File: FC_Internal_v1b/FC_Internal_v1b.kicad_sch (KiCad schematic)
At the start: 97 parts, among them IC1 RP2040_QFN56, IC2 AZ1117CH-3.3TRG1, J1 Conn_ARM_JTAG_SWD_10, J10 BM04B-SRSS-TB(LF)(SN), J11 BM04B-SRSS-TB(LF)(SN), J12 BM04B-SRSS-TB(LF)(SN), J13 Breakout, J15 Battery, J15 Breakout, J16 Debug, J2 FC to EPS Connector, J3 Life Makes Lemonade, J4 104031-0811, J5 BM04B-SRSS-TB(LF)(SN), J6 Conn_Coaxial, J7 Breakout, J8 USB_B_Micro, J9 BM04B-SRSS-TB(LF)(SN), SW1 KMR2, SW2 KMR2, U10 AP3602AKTR-G1, U3 MAX706RESA, U4 RFM98PW, U5 RFM9xBreakout, U6 W25Q128JV, U7 LSM6DSOTR, U8 LSM303AGRTR, U9 MCP25625-E/ML, Y1 12MHZ, Y3 16MHZ 12 pf

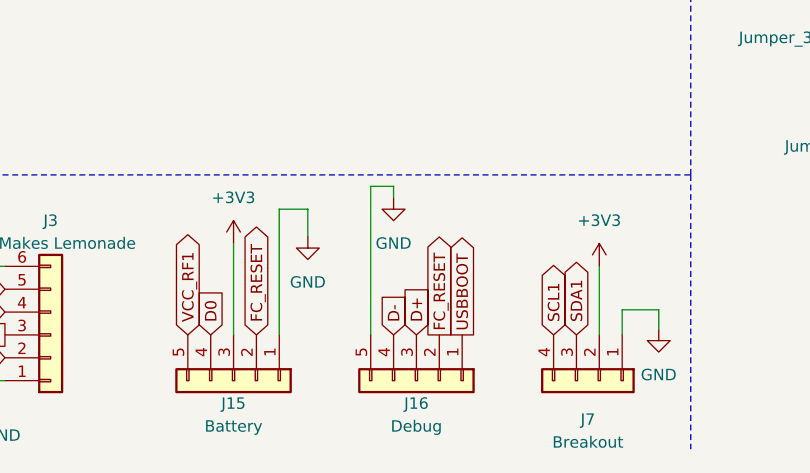
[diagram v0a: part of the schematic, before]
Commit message: Added 5pos Debug Connector to Layout
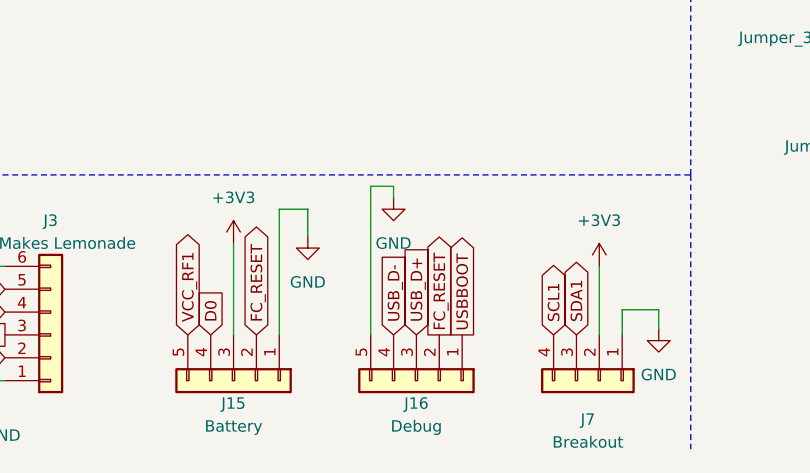
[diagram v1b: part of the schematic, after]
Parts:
- J7: footprint Connector_JST:JST_SH_SM04B-SRSS-TB_1x04-1MP_P1.00mm_Horizontal -> FC_DEV_BOARD:JST_BM04B-SRSS-TB(LF)(SN)
- J9: footprint FC_DEV_BOARD:JST_BM04B-SRSS-TB(LF)(SN) -> FC_DEV_BOARD:JST_BM04B-SRSS-TB(LF)(SN)
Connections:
- net D+: no longer J16.3 (Pin_3)
- net D-: no longer J16.4 (Pin_4)
- net USB_D+: now also J16.3 (Pin_3)
- net USB_D-: now also J16.4 (Pin_4)
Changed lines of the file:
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@@
 		)
 	)
-	(global_label "D-"
+	(global_label "USB_D-"
 		(shape input)
 		(at 156.21 271.78 90)
@@
 		)
 		(property "Intersheetrefs" "${INTERSHEET_REFS}"
-			(at 156.21 265.9524 90)
+			(at 156.21 261.1748 90)
 			(effects
 				(font
@@
 		)
 	)
-	(global_label "D+"
+	(global_label "USB_D+"
 		(shape input)
 		(at 158.75 271.78 90)
@@
 		)
 		(property "Intersheetrefs" "${INTERSHEET_REFS}"
-			(at 158.75 265.9524 90)
+			(at 158.75 261.1748 90)
 			(effects
 				(font
@@
 			)
 		)
-		(property "Footprint" "Connector_JST:JST_SH_SM04B-SRSS-TB_1x04-1MP_P1.00mm_Horizontal"
+		(property "Footprint" "FC_DEV_BOARD:JST_BM04B-SRSS-TB(LF)(SN)"
 			(at 179.07 276.86 0)
 			(effects
@@
 			)
 		)
-		(property "Footprint" "FC_DEV_BOARD:JST_BM04B-SRSS-TB(LF)(SN)"
+		(property "Footprint" "FC_DEV_BOARD:JST_BM04B-SRSS-TB(LF)(SN) "
 			(at 181.61 63.5 0)
 			(effects

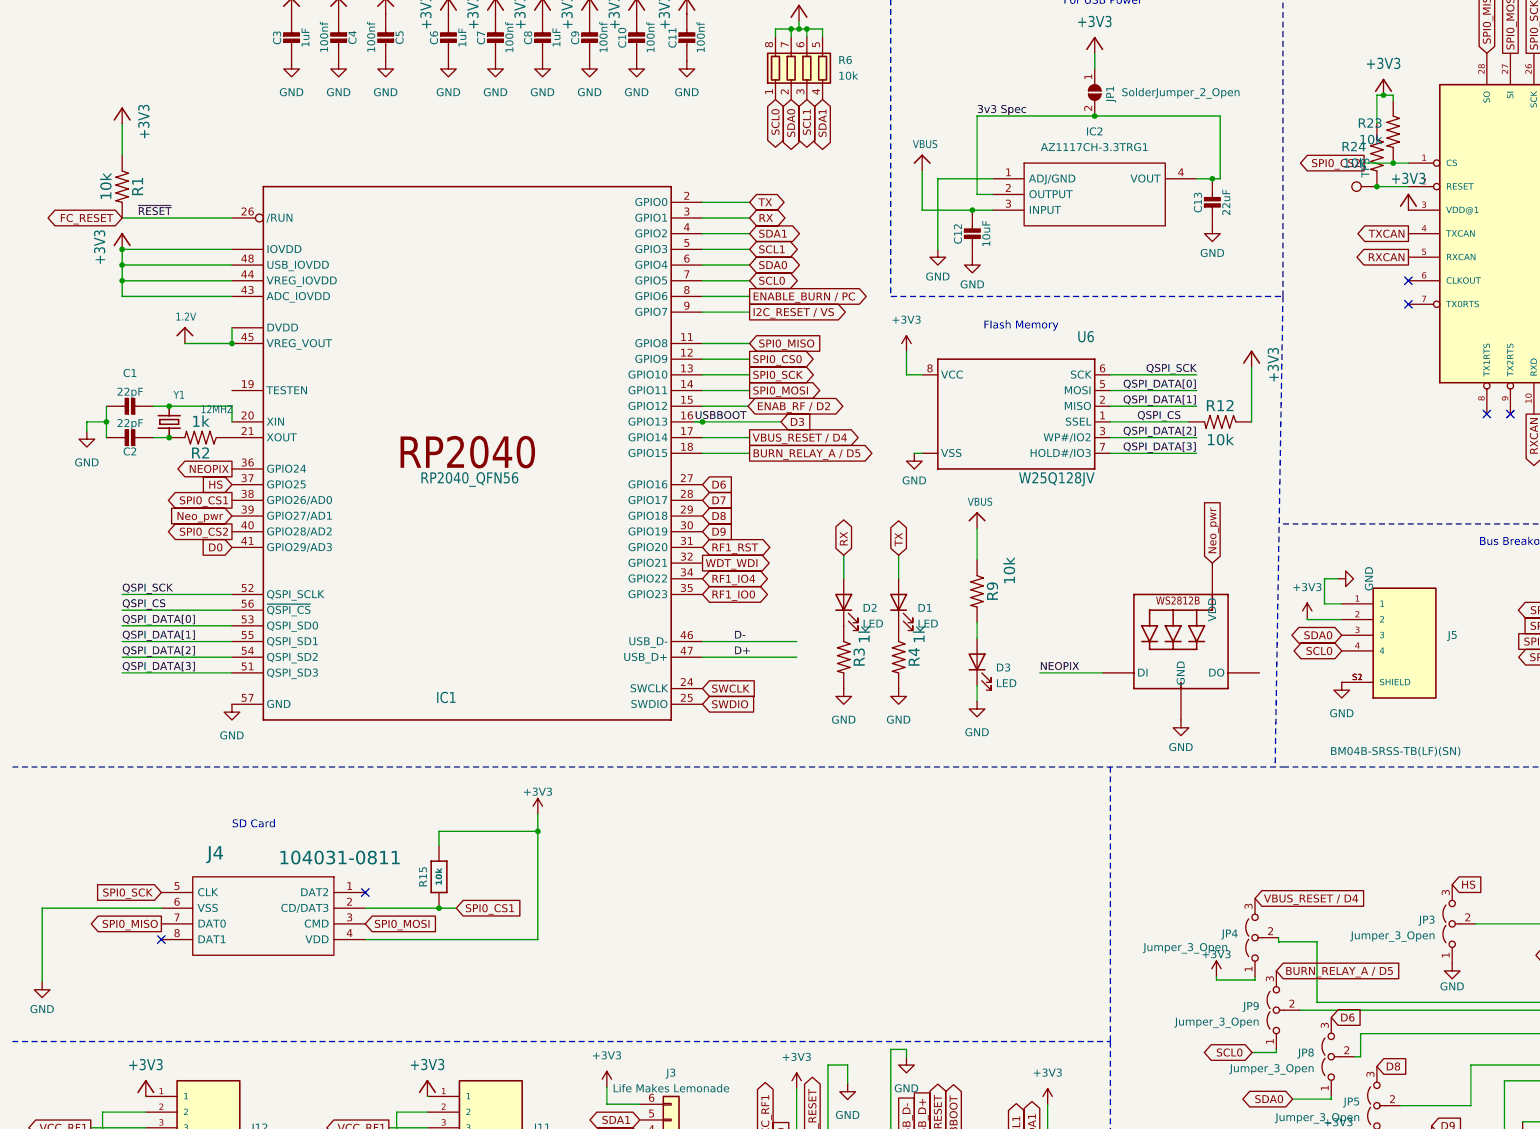
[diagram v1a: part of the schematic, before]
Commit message: Finished Schematic Capture for New SD Card Holder
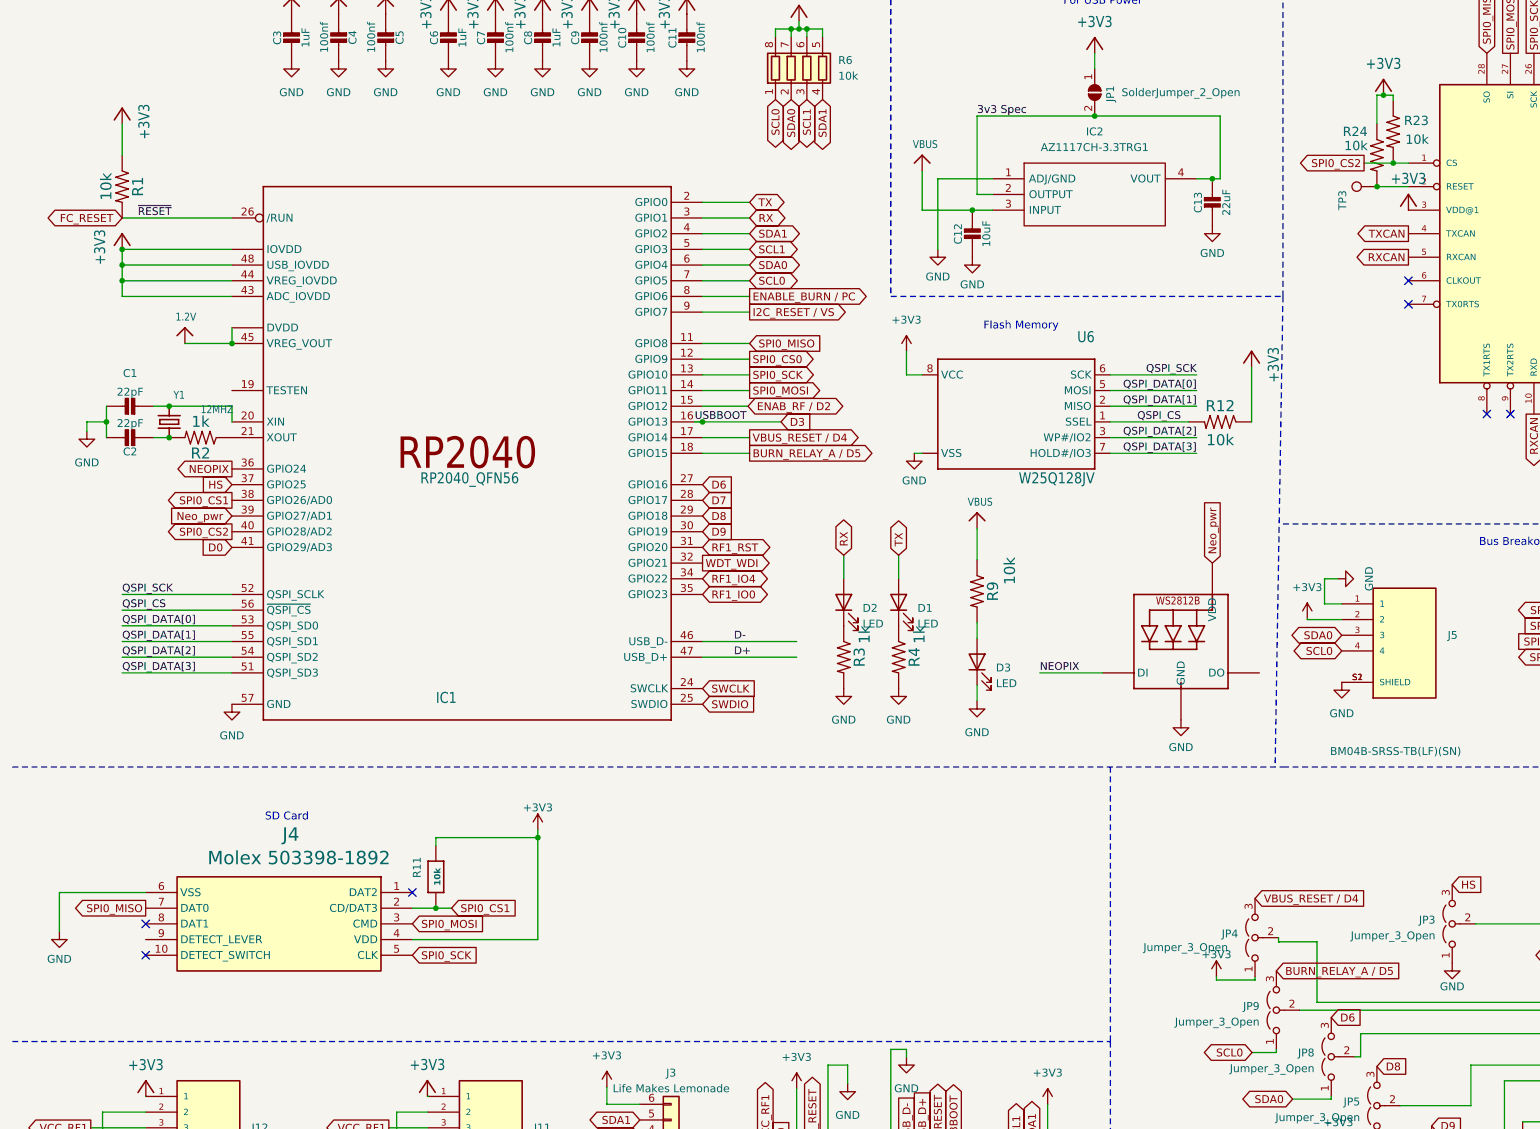
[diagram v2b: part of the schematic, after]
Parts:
- removed R15: 10k, Resistor_SMD:R_0402_1005Metric, symbol Adafruit ItsyBitsy RP2040-eagle-import:RESISTOR_0402NO
- added R11: 10k, Resistor_SMD:R_0402_1005Metric, symbol Adafruit ItsyBitsy RP2040-eagle-import:RESISTOR_0402NO
- J4: value 104031-0811 -> Molex 503398-1892; footprint Connector_Card:microSD_HC_Molex_104031-0811 -> 503398-1892-1; symbol Molex_SD:104031-0811 -> Molex 503398-1892:503398-1892; Manufacturer_Part_Number 104031-0811 -> 503398-1892; Mouser Part Number 538-104031-0811 -> 538-503398-1892; Mouser Price/Stock https://www.mouser.co.uk/ProductDetail/Molex/104031-0811?qs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 -> https://www.mouser.co.uk/ProductDetail/Molex/503398-1892?qs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
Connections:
- net +3V3: now also R11.2
- net SPI0_CS1: now also R11.1
- no-connect marks 33 -> 34

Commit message: Finished Adding SD Card To Layout
Also moved the SD card to more convenient slot
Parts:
- added H1, H2: MountingHole, symbol Mechanical:MountingHole
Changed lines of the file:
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@@
+	)
+	(symbol
+		(lib_id "Mechanical:MountingHole")
+		(at 167.64 241.3 0)
+		(unit 1)
+		(exclude_from_sim yes)
+		(in_bom no)
+		(on_board yes)
+		(dnp no)
+		(fields_autoplaced yes)
+		(property "Reference" "H1"
+			(at 170.18 240.0299 0)
+			(effects
+				(font
+					(size 1.27 1.27)
+				)
+				(justify left)
+			)
+		)
+		(property "Value" "MountingHole"
+			(at 170.18 242.5699 0)
+			(effects
+				(font
+					(size 1.27 1.27)
+				)
+				(justify left)
+			)
+		)
+		(property "Footprint" ""
+			(at 167.64 241.3 0)
+			(effects
+				(font
+					(size 1.27 1.27)
+				)
+				(hide yes)
+			)
+		)
+		(property "Datasheet" "~"
+			(at 167.64 241.3 0)
+			(effects
+				(font
+					(size 1.27 1.27)
+				)
+				(hide yes)
+			)
+		)
+		(property "Description" "Mounting Hole without connection"
+			(at 167.64 241.3 0)
+			(effects
+				(font
+					(size 1.27 1.27)
+				)
+				(hide yes)
+			)
+		)
+		(instances
+			(project "FC_Internal_v1b"
+				(path "/c64c0d72-a9f6-4f3a-891e-1f647558f538"
+					(reference "H1")
+					(unit 1)
+				)
+			)
+		)
 	)
 	(symbol
@@
 					(unit 1)
 				)
+			)
+		)
+	)
+	(symbol
+		(lib_id "Mechanical:MountingHole")
+		(at 167.64 247.65 0)
+		(unit 1)
+		(exclude_from_sim yes)
+		(in_bom no)
+		(on_board yes)
+		(dnp no)
+		(fields_autoplaced yes)
+		(property "Reference" "H2"
+			(at 170.18 246.3799 0)
+			(effects
+				(font
+					(size 1.27 1.27)
+				)
+				(justify left)
+			)
+		)
+		(property "Value" "MountingHole"
+			(at 170.18 248.9199 0)
+			(effects
+				(font
+					(size 1.27 1.27)
+				)
+				(justify left)
+			)
+		)
+		(property "Footprint" ""
+			(at 167.64 247.65 0)
+			(effects
+				(font
+					(size 1.27 1.27)
+				)
+				(hide yes)
+			)
+		)
+		(property "Datasheet" "~"
+			(at 167.64 247.65 0)
+			(effects
+				(font
+					(size 1.27 1.27)
+				)
+				(hide yes)
+			)
+		)
+		(property "Description" "Mounting Hole without connection"
+			(at 167.64 247.65 0)
+			(effects
+				(font
+					(size 1.27 1.27)
+				)
+				(hide yes)
+			)
+		)
+		(instances
+			(project "FC_Internal_v1b"
+				(path "/c64c0d72-a9f6-4f3a-891e-1f647558f538"
+					(reference "H2")
+					(unit 1)
+				)

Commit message: Finished First Pass Retracing
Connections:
- net GND: now also IC1.19 (TESTEN)
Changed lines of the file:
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@@
 	(wire
 		(pts
+			(xy 22.86 142.24) (xy 22.86 144.78)
+		)
+		(stroke
+			(width 0)
+			(type default)
+		)
+	)
+	(wire
+		(pts
 			(xy 397.002 44.45) (xy 397.002 46.99)
 		)
@@
 	(wire
 		(pts
+			(xy 46.99 148.59) (xy 40.64 148.59)
+		)
+		(stroke
+			(width 0)
+			(type default)
+		)
+	)
+	(wire
+		(pts
+			(xy 40.64 148.59) (xy 40.64 142.24)
+		)
+		(stroke
+			(width 0)
+			(type default)
+		)
+	)
+	(wire
+		(pts
 			(xy 181.61 268.986) (xy 185.674 268.986)
 		)
@@
 	(wire
 		(pts
+			(xy 40.64 142.24) (xy 22.86 142.24)
+		)
+		(stroke
+			(width 0)
+			(type default)
+		)
+	)
+	(wire
+		(pts
 			(xy 273.05 93.1164) (xy 273.05 93.98)
 		)
@@
 			)
 		)
-		(property "Datasheet" ""
+		(property "Datasheet" "https://datasheets.raspberrypi.com/rp2040/rp2040-datasheet.pdf"
 			(at 85.09 158.75 0)
 			(effects
@@
 					(unit 1)
 				)
+			)
+		)
+	)
+	(symbol
+		(lib_id "power:GND")
+		(at 22.86 144.78 0)
+		(unit 1)
+		(exclude_from_sim no)
+		(in_bom yes)
+		(on_board yes)
+		(dnp no)
+		(fields_autoplaced yes)
+		(property "Reference" "#PWR041"
+			(at 22.86 151.13 0)
+			(effects
+				(font
+					(size 1.27 1.27)
+				)
+				(hide yes)
+			)
+		)
+		(property "Value" "GND"
+			(at 22.86 149.86 0)
+			(effects
+				(font
+					(size 1.27 1.27)
+				)
+			)
+		)
+		(property "Footprint" ""
+			(at 22.86 144.78 0)
+			(effects
+				(font
+					(size 1.27 1.27)
+				)
+				(hide yes)
+			)
+		)
+		(property "Datasheet" ""
+			(at 22.86 144.78 0)
+			(effects
+				(font
+					(size 1.27 1.27)
+				)
+				(hide yes)
+			)
+		)
+		(property "Description" ""
+			(at 22.86 144.78 0)
+			(effects
+				(font
+					(size 1.27 1.27)
+				)
+				(hide yes)
+			)
+		)
+		(pin "1"
+		)
+		(instances
+			(project "FC_Internal_v1b"
+				(path "/c64c0d72-a9f6-4f3a-891e-1f647558f538"
+					(reference "#PWR041")
+					(unit 1)
+				)

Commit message: Added Footprint for RTC
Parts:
- added C17: CPH3225A, SuperCap:CPH3225A, symbol CPH3225A:CPH3225A
- added IC3: RV-3028-C7_32.768kHz_1ppm_TA_QC, RTC:RV3028C7, symbol RV-3028-C7:RV-3028-C7_32.768kHz_1ppm_TA_QC
